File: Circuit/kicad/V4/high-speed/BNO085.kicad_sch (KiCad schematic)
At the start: 9 parts, among them U57 BNO080, Y4 32.768MHz

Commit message: high speed first step
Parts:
- renumbered C109 to C45, C108 to C46, C112 to C47, C113 to C48, C110 to C49, C111 to C50, CT7 to CT6, U57 to U22, Y4 to Y2
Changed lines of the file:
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@@
 		(dnp no)
 		(fields_autoplaced yes)
-		(property "Reference" "C111"
+		(property "Reference" "C50"
 			(at 139.7 86.3599 0)
 			(effects
@@
 		)
 		(instances
-			(project "CM5IO"
-				(path "/e63e39d7-6ac0-4ffd-8aa3-1841a4541b55/a83afe30-5c7e-43cb-a5b2-f6f97a0812b3/86209e6a-92ae-4699-a125-02d46b525fc7/e860c21c-cbfd-40eb-8548-00ff1d3dbc30"
-					(reference "C111")
+			(project "high-speed"
+				(path "/e63e39d7-6ac0-4ffd-8aa3-1841a4541b55/a83afe30-5c7e-43cb-a5b2-f6f97a0812b3/44b38683-f103-4ae7-96a1-9a48eb7831e7"
+					(reference "C50")
 					(unit 1)
 				)
@@
 		(dnp no)
 		(fields_autoplaced yes)
-		(property "Reference" "C110"
+		(property "Reference" "C49"
 			(at 127 86.3599 0)
 			(effects
@@
 		)
 		(instances
-			(project "CM5IO"
-				(path "/e63e39d7-6ac0-4ffd-8aa3-1841a4541b55/a83afe30-5c7e-43cb-a5b2-f6f97a0812b3/86209e6a-92ae-4699-a125-02d46b525fc7/e860c21c-cbfd-40eb-8548-00ff1d3dbc30"
-					(reference "C110")
+			(project "high-speed"
+				(path "/e63e39d7-6ac0-4ffd-8aa3-1841a4541b55/a83afe30-5c7e-43cb-a5b2-f6f97a0812b3/44b38683-f103-4ae7-96a1-9a48eb7831e7"
+					(reference "C49")
 					(unit 1)
 				)
@@
 		(on_board yes)
 		(dnp no)
-		(property "Reference" "#PWR0153"
+		(property "Reference" "#PWR0141"
 			(at 118.11 59.69 0)
 			(effects
@@
 		)
 		(instances
-			(project "CM5IO"
-				(path "/e63e39d7-6ac0-4ffd-8aa3-1841a4541b55/a83afe30-5c7e-43cb-a5b2-f6f97a0812b3/86209e6a-92ae-4699-a125-02d46b525fc7/e860c21c-cbfd-40eb-8548-00ff1d3dbc30"
-					(reference "#PWR0153")
+			(project "high-speed"
+				(path "/e63e39d7-6ac0-4ffd-8aa3-1841a4541b55/a83afe30-5c7e-43cb-a5b2-f6f97a0812b3/44b38683-f103-4ae7-96a1-9a48eb7831e7"
+					(reference "#PWR0141")
 					(unit 1)
 				)
@@
 		(dnp no)
 		(fields_autoplaced yes)
-		(property "Reference" "CT7"
+		(property "Reference" "CT6"
 			(at 152.4 85.8138 0)
 			(effects
@@
 		)
 		(instances
-			(project "CM5IO"
-				(path "/e63e39d7-6ac0-4ffd-8aa3-1841a4541b55/a83afe30-5c7e-43cb-a5b2-f6f97a0812b3/86209e6a-92ae-4699-a125-02d46b525fc7/e860c21c-cbfd-40eb-8548-00ff1d3dbc30"
-					(reference "CT7")
+			(project "high-speed"
+				(path "/e63e39d7-6ac0-4ffd-8aa3-1841a4541b55/a83afe30-5c7e-43cb-a5b2-f6f97a0812b3/44b38683-f103-4ae7-96a1-9a48eb7831e7"
+					(reference "CT6")
 					(unit 1)
 				)
@@
 		(on_board yes)
 		(dnp no)
-		(property "Reference" "#U$01"
+		(property "Reference" "#U$02"
 			(at 45.72 54.61 0)
 			(effects
@@
 		)
 		(instances
-			(project "CM5IO"
-				(path "/e63e39d7-6ac0-4ffd-8aa3-1841a4541b55/a83afe30-5c7e-43cb-a5b2-f6f97a0812b3/86209e6a-92ae-4699-a125-02d46b525fc7/e860c21c-cbfd-40eb-8548-00ff1d3dbc30"
-					(reference "#U$01")
+			(project "high-speed"
+				(path "/e63e39d7-6ac0-4ffd-8aa3-1841a4541b55/a83afe30-5c7e-43cb-a5b2-f6f97a0812b3/44b38683-f103-4ae7-96a1-9a48eb7831e7"
+					(reference "#U$02")
 					(unit 1)
 				)
@@
 		(on_board yes)
 		(dnp no)
-		(property "Reference" "C112"
+		(property "Reference" "C47"
 			(at 155.19 60.98 90)
 			(effects
@@
 		)
 		(instances
-			(project "CM5IO"
-				(path "/e63e39d7-6ac0-4ffd-8aa3-1841a4541b55/a83afe30-5c7e-43cb-a5b2-f6f97a0812b3/86209e6a-92ae-4699-a125-02d46b525fc7/e860c21c-cbfd-40eb-8548-00ff1d3dbc30"
-					(reference "C112")
+			(project "high-speed"
+				(path "/e63e39d7-6ac0-4ffd-8aa3-1841a4541b55/a83afe30-5c7e-43cb-a5b2-f6f97a0812b3/44b38683-f103-4ae7-96a1-9a48eb7831e7"
+					(reference "C47")
 					(unit 1)
 				)
@@
 		(on_board yes)
 		(dnp no)
-		(property "Reference" "Y4"
+		(property "Reference" "Y2"
 			(at 165.1 48.895 0)
 			(effects
@@
 		)
 		(instances
-			(project "CM5IO"
-				(path "/e63e39d7-6ac0-4ffd-8aa3-1841a4541b55/a83afe30-5c7e-43cb-a5b2-f6f97a0812b3/86209e6a-92ae-4699-a125-02d46b525fc7/e860c21c-cbfd-40eb-8548-00ff1d3dbc30"
-					(reference "Y4")
+			(project "high-speed"
+				(path "/e63e39d7-6ac0-4ffd-8aa3-1841a4541b55/a83afe30-5c7e-43cb-a5b2-f6f97a0812b3/44b38683-f103-4ae7-96a1-9a48eb7831e7"
+					(reference "Y2")
 					(unit 1)
 				)
@@
 		(on_board yes)
 		(dnp no)
-		(property "Reference" "#PWR0152"
+		(property "Reference" "#PWR0144"
 			(at 68.58 86.36 0)
 			(effects
@@
 		)
 		(instances
-			(project "CM5IO"
-				(path "/e63e39d7-6ac0-4ffd-8aa3-1841a4541b55/a83afe30-5c7e-43cb-a5b2-f6f97a0812b3/86209e6a-92ae-4699-a125-02d46b525fc7/e860c21c-cbfd-40eb-8548-00ff1d3dbc30"
-					(reference "#PWR0152")
+			(project "high-speed"
+				(path "/e63e39d7-6ac0-4ffd-8aa3-1841a4541b55/a83afe30-5c7e-43cb-a5b2-f6f97a0812b3/44b38683-f103-4ae7-96a1-9a48eb7831e7"
+					(reference "#PWR0144")
 					(unit 1)
 				)
@@
 		(on_board yes)
 		(dnp no)
-		(property "Reference" "C109"
+		(property "Reference" "C45"
 			(at 118.09 34.54 90)
 			(effects
@@
 		)
 		(instances
-			(project "CM5IO"
-				(path "/e63e39d7-6ac0-4ffd-8aa3-1841a4541b55/a83afe30-5c7e-43cb-a5b2-f6f97a0812b3/86209e6a-92ae-4699-a125-02d46b525fc7/e860c21c-cbfd-40eb-8548-00ff1d3dbc30"
-					(reference "C109")
+			(project "high-speed"
+				(path "/e63e39d7-6ac0-4ffd-8aa3-1841a4541b55/a83afe30-5c7e-43cb-a5b2-f6f97a0812b3/44b38683-f103-4ae7-96a1-9a48eb7831e7"
+					(reference "C45")
 					(unit 1)
 				)
@@
 		(on_board yes)
 		(dnp no)
-		(property "Reference" "C108"
+		(property "Reference" "C46"
 			(at 43.43 45.74 90)
 			(effects
@@
 		)
 		(instances
-			(project "CM5IO"
-				(path "/e63e39d7-6ac0-4ffd-8aa3-1841a4541b55/a83afe30-5c7e-43cb-a5b2-f6f97a0812b3/86209e6a-92ae-4699-a125-02d46b525fc7/e860c21c-cbfd-40eb-8548-00ff1d3dbc30"
-					(reference "C108")
+			(project "high-speed"
+				(path "/e63e39d7-6ac0-4ffd-8aa3-1841a4541b55/a83afe30-5c7e-43cb-a5b2-f6f97a0812b3/44b38683-f103-4ae7-96a1-9a48eb7831e7"
+					(reference "C46")
 					(unit 1)
 				)
@@
 		(on_board yes)
 		(dnp no)
-		(property "Reference" "#PWR0151"
+		(property "Reference" "#PWR0142"
 			(at 46.99 67.31 0)
 			(effects
@@
 		)
 		(instances
-			(project "CM5IO"
-				(path "/e63e39d7-6ac0-4ffd-8aa3-1841a4541b55/a83afe30-5c7e-43cb-a5b2-f6f97a0812b3/86209e6a-92ae-4699-a125-02d46b525fc7/e860c21c-cbfd-40eb-8548-00ff1d3dbc30"
-					(reference "#PWR0151")
+			(project "high-speed"
+				(path "/e63e39d7-6ac0-4ffd-8aa3-1841a4541b55/a83afe30-5c7e-43cb-a5b2-f6f97a0812b3/44b38683-f103-4ae7-96a1-9a48eb7831e7"
+					(reference "#PWR0142")
 					(unit 1)
 				)
@@
 		(on_board yes)
 		(dnp no)
-		(property "Reference" "#PWR0154"
+		(property "Reference" "#PWR0145"
 			(at 149.86 100.33 0)
 			(effects
@@
 		)
 		(instances
-			(project "CM5IO"
-				(path "/e63e39d7-6ac0-4ffd-8aa3-1841a4541b55/a83afe30-5c7e-43cb-a5b2-f6f97a0812b3/86209e6a-92ae-4699-a125-02d46b525fc7/e860c21c-cbfd-40eb-8548-00ff1d3dbc30"
-					(reference "#PWR0154")
+			(project "high-speed"
+				(path "/e63e39d7-6ac0-4ffd-8aa3-1841a4541b55/a83afe30-5c7e-43cb-a5b2-f6f97a0812b3/44b38683-f103-4ae7-96a1-9a48eb7831e7"
+					(reference "#PWR0145")
 					(unit 1)
 				)
@@
 		(on_board yes)
 		(dnp no)
-		(property "Reference" "U57"
+		(property "Reference" "U22"
 			(at 73.66 27.94 0)
 			(effects
@@
 		)
 		(instances
-			(project "CM5IO"
-				(path "/e63e39d7-6ac0-4ffd-8aa3-1841a4541b55/a83afe30-5c7e-43cb-a5b2-f6f97a0812b3/86209e6a-92ae-4699-a125-02d46b525fc7/e860c21c-cbfd-40eb-8548-00ff1d3dbc30"
-					(reference "U57")
+			(project "high-speed"
+				(path "/e63e39d7-6ac0-4ffd-8aa3-1841a4541b55/a83afe30-5c7e-43cb-a5b2-f6f97a0812b3/44b38683-f103-4ae7-96a1-9a48eb7831e7"
+					(reference "U22")
 					(unit 1)
 				)
@@
 		(on_board yes)
 		(dnp no)
-		(property "Reference" "C113"
+		(property "Reference" "C48"
 			(at 170.43 60.98 90)
 			(effects
@@
 		)
 		(instances
-			(project "CM5IO"
-				(path "/e63e39d7-6ac0-4ffd-8aa3-1841a4541b55/a83afe30-5c7e-43cb-a5b2-f6f97a0812b3/86209e6a-92ae-4699-a125-02d46b525fc7/e860c21c-cbfd-40eb-8548-00ff1d3dbc30"
-					(reference "C113")
+			(project "high-speed"
+				(path "/e63e39d7-6ac0-4ffd-8aa3-1841a4541b55/a83afe30-5c7e-43cb-a5b2-f6f97a0812b3/44b38683-f103-4ae7-96a1-9a48eb7831e7"
+					(reference "C48")
 					(unit 1)
 				)
@@
 		(on_board yes)
 		(dnp no)
-		(property "Reference" "#PWR0155"
+		(property "Reference" "#PWR0143"
 			(at 172.72 73.66 0)
 			(effects
@@
 		)
 		(instances
-			(project "CM5IO"
-				(path "/e63e39d7-6ac0-4ffd-8aa3-1841a4541b55/a83afe30-5c7e-43cb-a5b2-f6f97a0812b3/86209e6a-92ae-4699-a125-02d46b525fc7/e860c21c-cbfd-40eb-8548-00ff1d3dbc30"
-					(reference "#PWR0155")
+			(project "high-speed"
+				(path "/e63e39d7-6ac0-4ffd-8aa3-1841a4541b55/a83afe30-5c7e-43cb-a5b2-f6f97a0812b3/44b38683-f103-4ae7-96a1-9a48eb7831e7"
+					(reference "#PWR0143")
 					(unit 1)
 				)
@@
 		(on_board yes)
 		(dnp no)
-		(property "Reference" "#U$02"
+		(property "Reference" "#U$01"
 			(at 124.46 39.37 0)
 			(effects
@@
 		)
 		(instances
-			(project "CM5IO"
-				(path "/e63e39d7-6ac0-4ffd-8aa3-1841a4541b55/a83afe30-5c7e-43cb-a5b2-f6f97a0812b3/86209e6a-92ae-4699-a125-02d46b525fc7/e860c21c-cbfd-40eb-8548-00ff1d3dbc30"
-					(reference "#U$02")
-					(unit 1)
-				)
+			(project "high-speed"
+				(path "/e63e39d7-6ac0-4ffd-8aa3-1841a4541b55/a83afe30-5c7e-43cb-a5b2-f6f97a0812b3/44b38683-f103-4ae7-96a1-9a48eb7831e7"
+					(reference "#U$01")
+					(unit 1)
+				)

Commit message: kicad: high speed V2.2 Circuit finish psu bom update
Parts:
- removed C45, C46: 0.1uF, Capacitor_SMD:C_0805_2012Metric, symbol CM5IO-eagle-import:CAP_CERAMIC0603_NO
- removed C47, C48: 22pF, Capacitor_SMD:C_0805_2012Metric, symbol CM5IO-eagle-import:CAP_CERAMIC0603_NO
- removed C49, C50: 1uf, Capacitor_SMD:C_0805_2012Metric, symbol Device:C
- removed CT6: 10uf, Capacitor_Tantalum_SMD:CP_EIA-3528-21_Kemet-B, symbol Device:C_Polarized_Small
- removed Y2: 32.768MHz, Crystal:Crystal_SMD_HC49-SD, symbol Device:Crystal
- added C42, C43, C45: 100nf, Capacitor_SMD:C_0805_2012Metric, symbol Device:C
- added C44: 1uf, Capacitor_SMD:C_0805_2012Metric, symbol Device:C
- added C46: 22nf c0g, Capacitor_SMD:C_0805_2012Metric, symbol Device:C
- added R97: 10k, Resistor_SMD:R_0805_2012Metric, symbol Device:R
- added TP12: bno_sda, TestPoint:TestPoint_Pad_D1.5mm, symbol Connector:TestPoint_Small
- added TP13: bno_scl, TestPoint:TestPoint_Pad_D1.5mm, symbol Connector:TestPoint_Small
- U23: renamed from U22; value BNO080 -> BNO085; Cikkszám (none) -> 100.490.92; Link (none) -> https://www.hestore.hu/prod_10049092.html
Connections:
- net 3V3: now also C43.1, C44.1, C45.1, C46.1, R97.2
- net GND: now also C42.2, C43.2, C44.2, C45.2, C46.2
- net at U23.15 (S_SCL): now also TP13.1
- net at U23.16 (S_SDA): now also TP12.1
- net BNO_BOOT: now reaches U23.4 (BOOTN)
- net CAP: no longer names the net of U23.9 (CAP)
- net CAP: now also C42.1
- net XIN renamed 32.768KHZ
- net XOUT: no longer names the net of U23.26 (CLKSEL1/XOUT32)
- new net BNO_RST: R97.1
- no-connect marks 3 -> 1

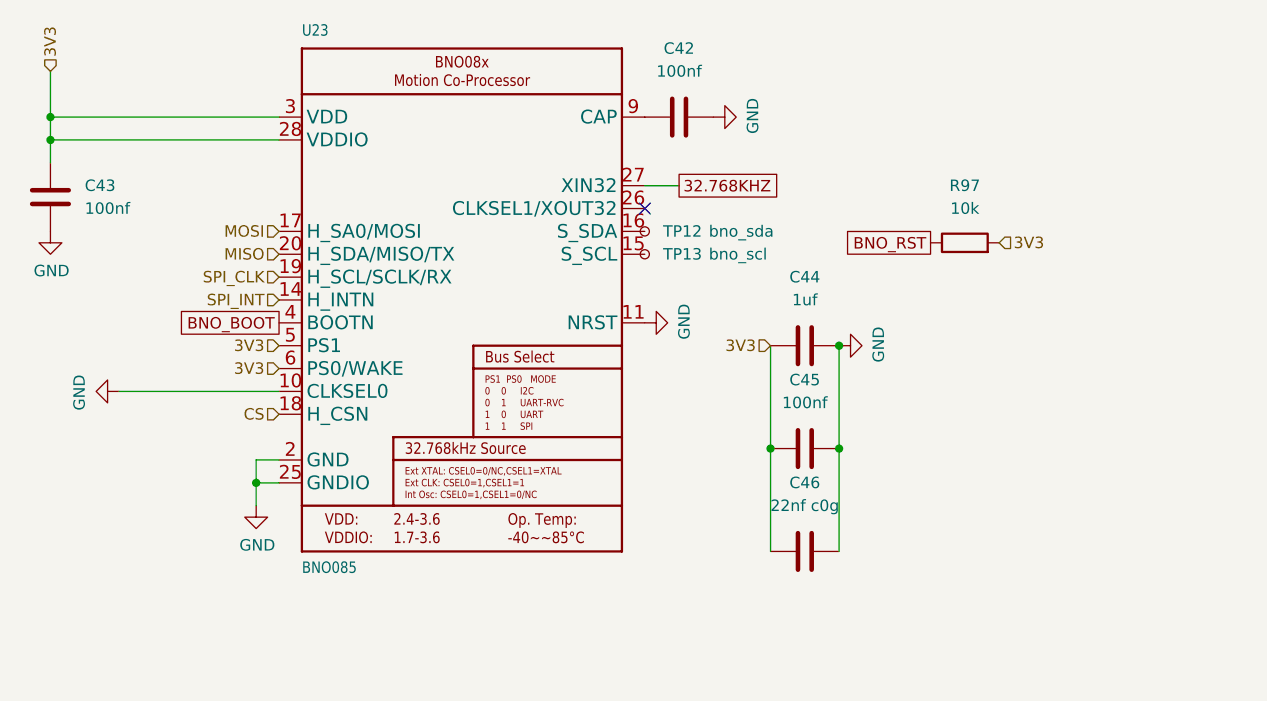
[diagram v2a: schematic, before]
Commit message: finished high-speed panel schematic and first try to doute gpios
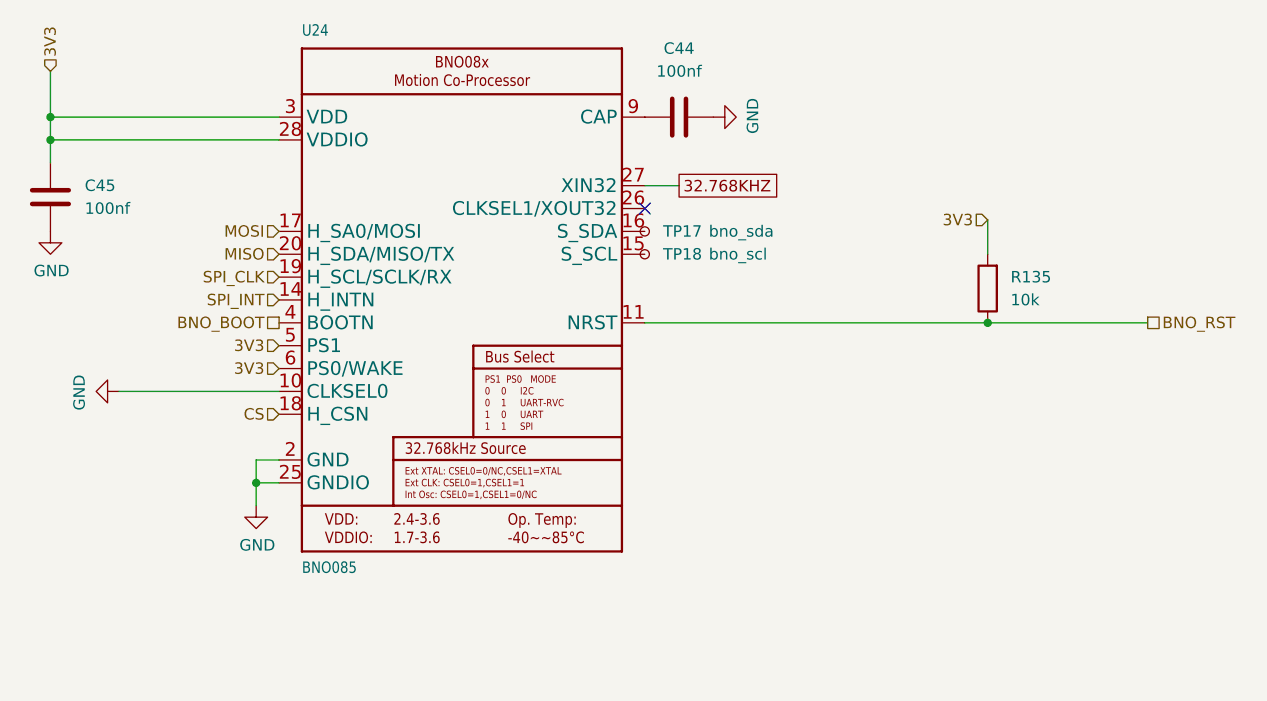
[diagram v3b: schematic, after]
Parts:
- removed C44: 1uf, Capacitor_SMD:C_0805_2012Metric, symbol Device:C
- removed C45: 100nf, Capacitor_SMD:C_0805_2012Metric, symbol Device:C
- removed C46: 22nf c0g, Capacitor_SMD:C_0805_2012Metric, symbol Device:C
- renumbered C42 to C44, C43 to C45, R97 to R135, TP12 to TP17, TP13 to TP18, U23 to U24
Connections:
- net BNO_RST: now also U24.11 (NRST)
- net GND: no longer U24.11 (NRST)
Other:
- moved on the sheet: R135
